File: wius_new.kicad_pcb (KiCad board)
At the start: 6 copper layers, 54 x 28 mm, 132 parts, among them IC1 BQ24040DSQT, J2 52746-1271, J3 1040310811, J4 SS5-10-3.00-L-D-K-TR, J5 USB4745-03-A, J8 2, J9 U.FL, M1 MountingHole_Pad, M2 MountingHole_Pad, M3 MountingHole_Pad, M4 MountingHole_Pad, SW3 Button Switch SPST-No, SW4 Button Switch SPST-No, U1 TPS62840YBGR, U12 SN74LVC1T45DCK, U13 TXB0104RUT, U2 TXB0104RUT, U3 SiWG917Y, U4 FT232HPQ, U5 LSM6DSV, U6 SN74AXC4T774RSVR, U7 SOIC_clipProgSmall, U8 SN74AXC4T774RSVR, U9 PCAL6408AHK, Y1 SIT1552AI-JE-DCC-32.768E

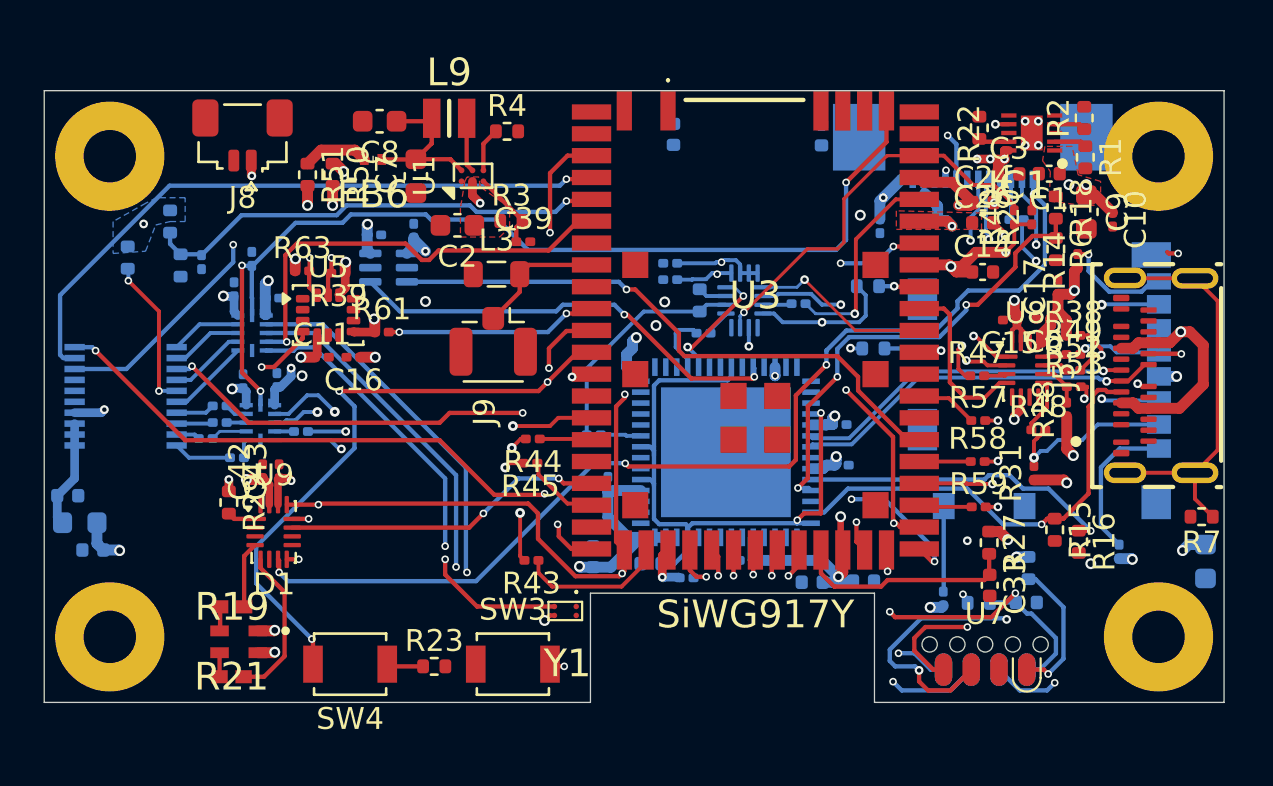
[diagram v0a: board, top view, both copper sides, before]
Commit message: updated eeprom and oscillator
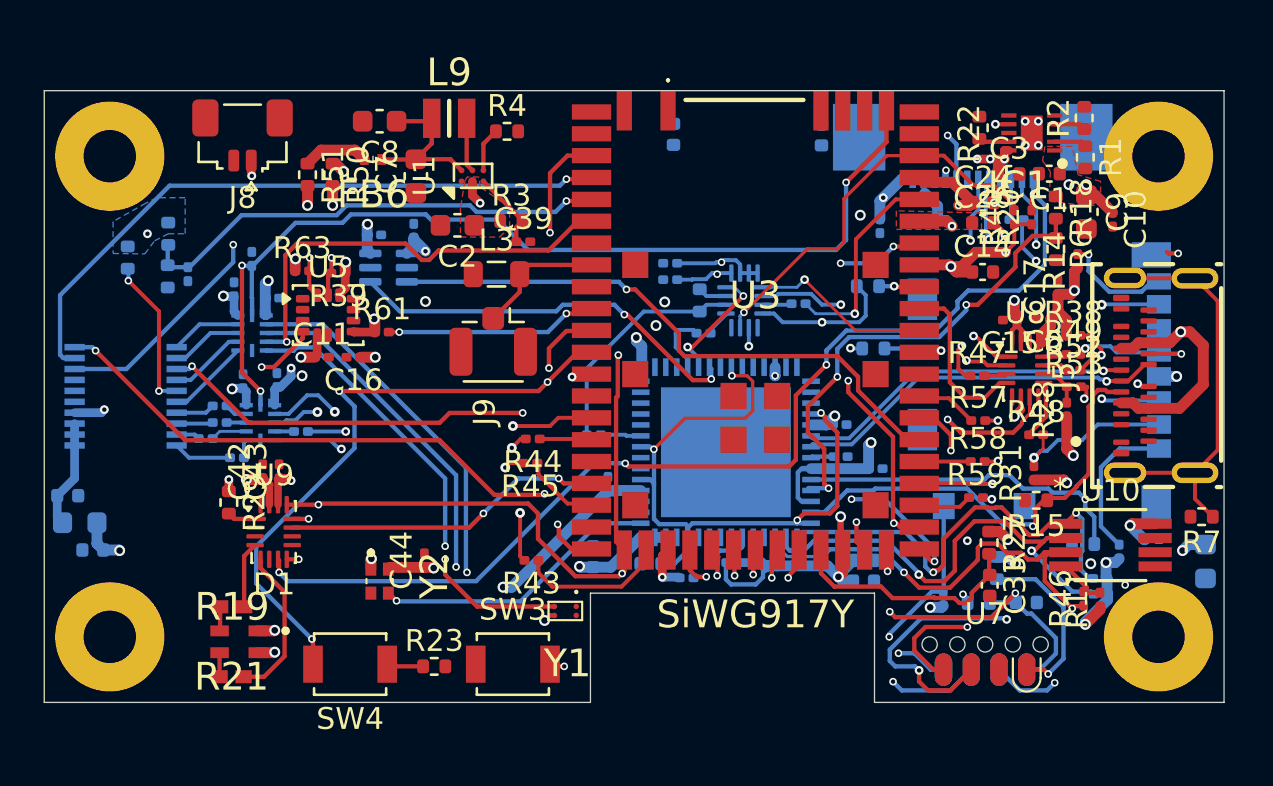
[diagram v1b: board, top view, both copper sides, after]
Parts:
- added C4: 1uF, Capacitor_SMD:C_0201_0603Metric, B.Cu at (173.7, 106.5)
- added C44: 100nF, Capacitor_SMD:C_0201_0603Metric, F.Cu at (140.4, 107.5)
- added R10: 10k, Resistor_SMD:R_0201_0603Metric, B.Cu at (171.3, 108.3)
- added R11: 10k, Resistor_SMD:R_0201_0603Metric, F.Cu at (171.3, 109.3)
- added R34: 10k, Resistor_SMD:R_0201_0603Metric, B.Cu at (171.3, 109.0)
- added R46: 2.2k, Resistor_SMD:R_0201_0603Metric, F.Cu at (170.6, 109.2)
- added R8: 10k, Resistor_SMD:R_0201_0603Metric, B.Cu at (153.9, 107.6)
- added R9: 12k, Resistor_SMD:R_0201_0603Metric, B.Cu at (159.4, 102.8)
- added U10: 93LC66B-I/MS, dz_mem:MSOP8_MC_MCH, F.Cu at (171.8, 106.8)
- added Y2: ASCO-12.000MHZ-EK-T3, dz_comm:ASCO16000MHZEKT, F.Cu at (138.3, 108.2)
- R16: moved to B.Cu
- moved C13 2.55 mm to (160.5, 107.5), turned to 0 degrees
- moved R15 1.60 mm to (168.4, 104.8), turned to 180 degrees
- moved C21 1.56 mm to (161.1, 103.3)
- moved R24 1.45 mm to (166.6, 107.8)
- moved C40 0.83 mm to (129.6, 94.4)
- moved R30 0.77 mm to (128.7, 94.5)
- moved R35 0.57 mm to (128.7, 92.5)
- moved R59 0.44 mm to (165.7, 104.6)
- moved R48 0.25 mm to (168.4, 101.8)
- moved R16 0.22 mm to (170.6, 106.8), turned to 180 degrees
- moved C22 0.22 mm to (155.3, 107.6)
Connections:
- U3 pad 43: unconnected-(U3C-GPIO_51-Pad43) -> /IMU_SD/INT_SD
- U4 pad 1: unconnected-(U4A-EECS-Pad1) -> /USB_FT232HPQ/EECS
- U4 pad 15: unconnected-(U4A-OSCI-Pad15) -> /USB_FT232HPQ/OSCI
- U4 pad 2: unconnected-(U4A-EECLK-Pad2) -> /USB_FT232HPQ/EECLK
- U4 pad 3: unconnected-(U4A-EEDATA-Pad3) -> /USB_FT232HPQ/EEDATA
- U4 pad 34: unconnected-(U4A-ACBUS2-Pad34) -> Net-(U12-B)
- U4 pad 38: Net-(U12-B) -> unconnected-(U4A-ACBUS5-Pad38)
- U4 pad 4: unconnected-(U4A-TEST-Pad4) -> GND
- U4 pad 50: unconnected-(U4A-REF-Pad50) -> Net-(U4A-REF)
- U4 pad 54: unconnected-(U4A-PD1_VCONN-Pad54) -> 3V3_VBUS
- U4 pad 6: unconnected-(U4A-RESET#-Pad6) -> Net-(U4A-RESET#)
- U9 pad 9: /IMU_SD/INT_SD -> unconnected-(U9-P6-Pad9)
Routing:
- net /IMU_SD/INT_SD: track 3.92 -> 33.6 mm, vias 0 -> 3
- net /IMU_SD/SD_EN: track 9.73 -> 34.9 mm, vias 2 -> 3
- net /USB_FT232HPQ/EECLK: track 0.00 -> 21.2 mm, vias 0 -> 2
- net /USB_FT232HPQ/EECS: track 0.00 -> 21.1 mm, vias 0 -> 2
- net /USB_FT232HPQ/EEDATA: track 0.00 -> 20.8 mm, vias 0 -> 2
- net 3V3_VBUS: track 73.7 -> 94.3 mm, vias 25 -> 30
- net /USB_FT232HPQ/OSCI: track 0.00 -> 13.2 mm, vias 0 -> 1
- net Net-(U10-DO): track 0.00 -> 2.37 mm
- net Net-(U4A-RESET#): track 0.00 -> 2.22 mm
- net Net-(U12-B): track 20.2 -> 18.3 mm
- net /USB_FT232HPQ/1V2: track 28.8 -> 30.4 mm, vias 2 -> 4
- net /IMU_SD/I2C_IMU.SDA: track 62.9 -> 64.4 mm
- net Net-(R24-Pad2): track 6.54 -> 7.99 mm
- net Net-(U4A-REF): track 0.00 -> 1.05 mm
- net /IMU_SD/I2C_IMU.SCL: track 67.7 -> 68.7 mm
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
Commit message: updated schematic and PCB
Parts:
- added REF**: Oscillator_SMD_Abracon_ASCO-4Pin_1.6x1.2mm, Oscillator:Oscillator_SMD_Abracon_ASCO-4Pin_1.6x1.2mm, B.Cu at (147.4, 105.3)
- moved C20 0.82 mm to (149.2, 104.7), turned to -90 degrees
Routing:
- net 3V3_VBUS: track 94.3 -> 88.2 mm, vias 30 -> 31
- net GND: track 1.00 -> 5.43 mm, vias 6 -> 8
- net /MCU/MCU_POWER_RF/POC_IN: track 34.2 -> 32.6 mm

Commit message: updated routing
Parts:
- removed REF**: Oscillator_SMD_Abracon_ASCO-4Pin_1.6x1.2mm, Oscillator:Oscillator_SMD_Abracon_ASCO-4Pin_1.6x1.2mm
- C44: moved to B.Cu
- Y2: footprint dz_comm:ASCO16000MHZEKT -> Oscillator:Oscillator_SMD_Abracon_ASCO-4Pin_1.6x1.2mm; moved to B.Cu
- moved Y2 9.77 mm to (147.7, 105.2)
- moved C44 6.67 mm to (147.0, 106.4), turned to 0 degrees
- moved C22 0.58 mm to (155.9, 107.7)
- moved R8 0.58 mm to (154.5, 107.6)
- moved R48 0.50 mm to (168.9, 101.8)
- moved C19 0.40 mm to (148.3, 107.7)
- moved C50 0.23 mm to (151.6, 88.0)
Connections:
- M1 pad 1: GNDA -> GND
- M2 pad 1: GNDA -> GND
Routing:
- net GND: track 5.43 -> 116.8 mm, vias 8 -> 140
- net /USB_FT232HPQ/OSCI: track 13.2 -> 2.21 mm, vias 1 -> 0
- net /USB_FT232HPQ/USB_CC2: track 32.3 -> 26.7 mm, vias 3 -> 2
- net /MCU/MCU_POWER_RF/POC_IN: track 32.6 -> 35.5 mm
- net 3V3_VBUS: track 88.2 -> 90.2 mm, vias 31 -> 29
- net /MCU/MCU_POWER_RF/POC_OUT: track 10.7 -> 9.71 mm
- net VBATTERY: track 8.73 -> 9.47 mm, vias 9 -> 8
- net Net-(U4A-RESET#): track 2.22 -> 1.51 mm
- net VIO: track 112.9 -> 112.3 mm
- added copper zone on In2.Cu, net GND

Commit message: final v1
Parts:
- moved C18 0.13 mm to (159.5, 101.2)
- moved C6 0.12 mm to (168.8, 96.3)
- moved R2 0.11 mm to (170.7, 87.2)
- moved R38 0.11 mm to (170.1, 97.1)
- moved J5 0.06 mm to (177.1, 99.1)
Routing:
- net VBATTERY: track 9.47 -> 12.9 mm, vias 8 -> 10
- net GND: track 116.8 -> 118.1 mm
- net VIO: track 112.3 -> 113.3 mm
- removed copper zone on B.Cu, net VBATTERY
- removed copper zone on F.Cu, net VBATTERY
- removed copper zone on F.Cu, net VIO
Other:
- board text added: "TINYPROBE_WIUS_v1 21/08/26 Samuele Savazzi"

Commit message: updated pcb file for rules
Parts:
- moved C50 1.54 mm to (150.5, 86.9), turned to 0 degrees
- moved C49 0.81 mm to (158.4, 87.2)
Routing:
- net GND: track 118.1 -> 116.9 mm, vias 140 -> 137
- net /IMU_SD/SPI_MCU.CS1: track 9.08 -> 8.31 mm
- net unconnected-(U3C-GPIO_54-Pad19): track 0.61 -> 0.00 mm
- net Net-(U3B-ANT_TUNE_1): track 0.00 -> 0.52 mm, vias 0 -> 1

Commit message: final v2
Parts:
- moved C50 0.06 mm to (150.4, 86.9)
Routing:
- net /MCU/MCU_POWER_RF/POC_IN: track 35.5 -> 34.0 mm
- net GND: track 116.9 -> 118.1 mm
- net VIO: track 113.2 -> 113.5 mm, vias 27 -> 24
- net 3V3_VBUS: track 90.5 -> 90.8 mm, vias 29 -> 28
- net Net-(U3B-ANT_TUNE_2): track 0.00 -> 0.28 mm, vias 0 -> 1
- net /USB_FT232HPQ/EEDATA: track 20.8 -> 20.7 mm, vias 2 -> 1
- net /IMU_SD/I2C_IMU.SDA: vias 5 -> 4
